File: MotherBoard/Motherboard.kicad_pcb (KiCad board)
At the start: 2 copper layers, 63.5 x 46.4 mm, 31 parts, among them J1 22-28-4157, J2 X6521WV-2x15H-C60D30, Q1 NCE2302, SW1 FSM4JSMATR, SW2 FSM4JSMATR, U1 ESP32 S3, U2 Unidirectional 5.5V 6V SOT-14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, U4 LIS2MDLTR, U5 LIS3DHTR, U6 MAX7219M/TR, U7 C193852

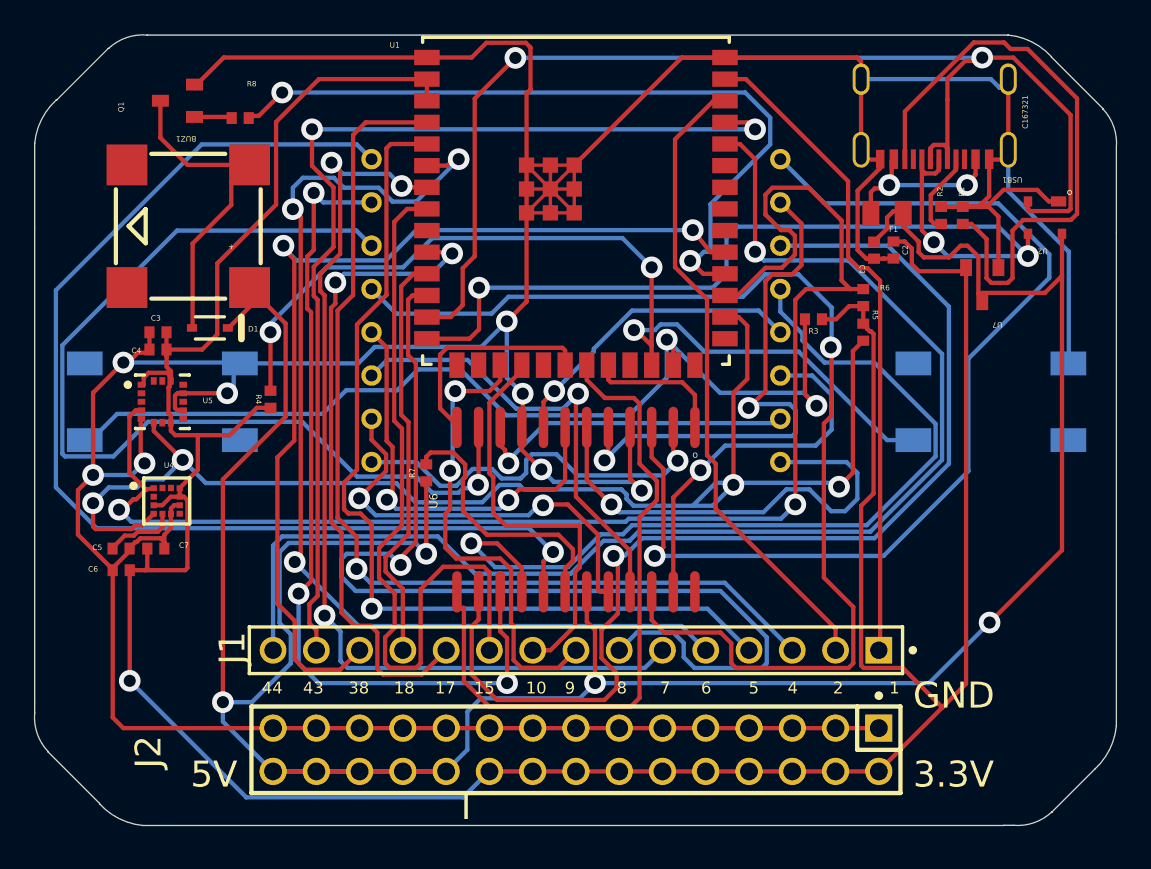
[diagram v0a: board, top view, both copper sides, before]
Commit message: motherboard imported and corrected
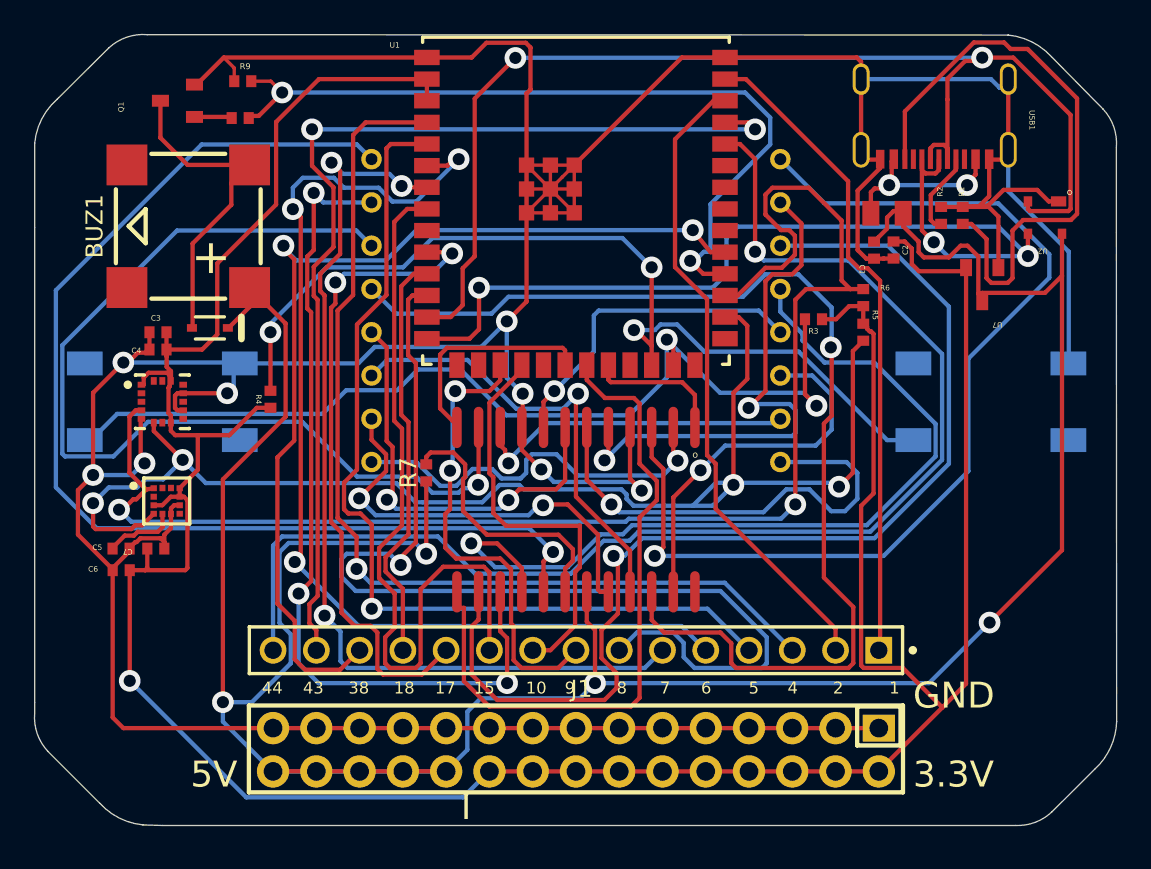
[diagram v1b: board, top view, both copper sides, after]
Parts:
- added R9: 10K, FableFootPrintLibrary:0402R, F.Cu at (129.0, 84.5)
- BUZ1: footprint BUZ-SMD_4P-L8.5-W8.5-P8.50-BR:BUZ-SMD_4P-L8.5-W8.5-P8.50-BR -> FableFootPrintLibrary:BUZ-SMD_4P-L8.5-W8.5-P8.50-BR
- C7: value 22pF -> 10uF
- D1: footprint Vault:DIOD-SOD323-2-A_V -> FableFootPrintLibrary:DIOD-SOD323-2-A_V
- F1: footprint Hub 2.0:0805 -> FableFootPrintLibrary:0805
- J1: footprint Vault:FP-22-28-4157-MFG -> FableFootPrintLibrary:FP-22-28-4157-MFG
- J2: footprint HDR-TH_30P-P2.54-V-M-R2-C15-S2.54-BL:HDR-TH_30P-P2.54-V-M-R2-C15-S2.54-BL -> FableFootPrintLibrary:HDR-TH_30P-P2.54-V-F-R2-C15-S2.54
- L1: footprint LED-SEG-TH_SZ421288N-64:LED-SEG-TH_SZ421288N-64 -> FableFootPrintLibrary:LED-SEG-TH_SZ421288N-64
- R7, R8: footprint Hub 2.0:0402R -> FableFootPrintLibrary:0402R
- SW1, SW2: footprint Vault:TECO-FSM4JSMATR_V -> FableFootPrintLibrary:TECO-FSM4JSMATR_V
- U4: footprint Vault:FP-LGA-12-DM00170568-MFG -> FableFootPrintLibrary:FP-LGA-12-DM00170568-MFG
- U5: footprint Vault:FP-LGA-16-7983231-MFG -> FableFootPrintLibrary:FP-LGA-16-7983231-MFG
- U6: footprint SOP-24_L15.4-W7.5-P1.27-LS10.4-BL:SOP-24_L15.4-W7.5-P1.27-LS10.4-BL -> FableFootPrintLibrary:SOP-24_L15.4-W7.5-P1.27-LS10.4-BL
- turned C7 to 180 degrees
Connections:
- net NetBUZ1_2 renamed Net-(D1-A)
- net NetC5_1 renamed Net-(U4-C1)
- net NetJ1_1 renamed /IO01
- net NetJ1_10 renamed /IO15
- net NetJ1_11 renamed /IO17
- net NetJ1_12 renamed /IO18
- net NetJ1_13 renamed /IO38
- net NetJ1_14 renamed /IO43
- net NetJ1_15 renamed /IO44
- net NetJ1_2 renamed /IO02
- net NetJ1_3 renamed /IO4
- net NetJ1_4 renamed /IO5
- net NetJ1_5 renamed /IO6
- net NetJ1_6 renamed /IO7
- net NetJ1_7 renamed /IO8
- net NetJ1_8 renamed /IO9
- net NetJ1_9 renamed /IO10
- net NetL1_1 renamed /DIG4
- net NetL1_10 renamed /SEGC
- net NetL1_11 renamed /SEGE
- net NetL1_12 renamed /DIG3
- net NetL1_13 renamed /SEGDP
- net NetL1_14 renamed /DIG1
- net NetL1_15 renamed /SEGF
- net NetL1_16 renamed /SEGG
- net NetL1_2 renamed /DIG6
- net NetL1_3 renamed /SEGA
- net NetL1_4 renamed /SEGB
- net NetL1_5 renamed /DIG7
- net NetL1_6 renamed /SEGD
- net NetL1_7 renamed /DIG5
- net NetL1_8 renamed /DIG2
- net NetL1_9 renamed /DIG0
- net NetQ1_1 renamed Net-(Q1-G)
- net NetR1_2 renamed Net-(USB1-CC2)
- net NetR2_2 renamed Net-(USB1-CC1)
- net NetR3_1 renamed /B1
- net NetR4_1 renamed /B2
- net NetR5_2 renamed /SDA
- net NetR6_2 renamed /SCL
- net NetR7_2 renamed Net-(U6-ISET)
- net NetR8_2 renamed /BUZZER_SIG
- net NetU1_19 renamed /IO11
- net NetU1_20 renamed /IO12
- net NetU1_21 renamed /IO13
- net NetU1_22 renamed /IO14
- net NetU1_9 renamed /IO16
- net fuse renamed /fuse
- BUZ1 pad 3: (no net) -> unconnected-(BUZ1-Pad3)
- BUZ1 pad 4: (no net) -> unconnected-(BUZ1-Pad4)
- C7 pad 1: +3.3 -> GND
- C7 pad 2: GND -> +3.3
- SW1 pad 2: (no net) -> unconnected-(SW1-Pad2)
- SW1 pad 3: (no net) -> unconnected-(SW1-Pad3)
- SW2 pad 2: (no net) -> unconnected-(SW2-Pad2)
- SW2 pad 3: (no net) -> unconnected-(SW2-Pad3)
- U1 pad 15: (no net) -> unconnected-(U1C-JTAG_SRC_(IO3)-Pad15)
- U1 pad 16: (no net) -> unconnected-(U1C-Boot_(IO46)-Pad16)
- U1 pad 23: (no net) -> unconnected-(U1A-IO21-Pad23)
- U1 pad 26: (no net) -> unconnected-(U1C-VDD_SPI_(IO45)-Pad26)
- U1 pad 27: (no net) -> unconnected-(U1C-Boot_(IO0)-Pad27)
- U1 pad 32: (no net) -> unconnected-(U1D-TCK_(IO39)-Pad32)
- U1 pad 33: (no net) -> unconnected-(U1D-TDO_(IO40)-Pad33)
- U1 pad 34: (no net) -> unconnected-(U1D-TDI_(IO41)-Pad34)
- U1 pad 35: (no net) -> unconnected-(U1D-TMS_(IO42)-Pad35)
- U4 pad 11: (no net) -> unconnected-(U4-NC-Pad11)
- U4 pad 12: (no net) -> unconnected-(U4-NC-Pad12)
- U4 pad 2: (no net) -> unconnected-(U4-NC-Pad2)
- U4 pad 7: (no net) -> unconnected-(U4-INT/DRDY/SDO-Pad7)
- U5 pad 11: (no net) -> unconnected-(U5-INT1-Pad11)
- U5 pad 13: (no net) -> unconnected-(U5-ADC3-Pad13)
- U5 pad 15: (no net) -> unconnected-(U5-ADC2-Pad15)
- U5 pad 16: (no net) -> unconnected-(U5-ADC1-Pad16)
- U5 pad 2: (no net) -> unconnected-(U5-NC-Pad2)
- U5 pad 3: (no net) -> unconnected-(U5-NC-Pad3)
- U5 pad 7: (no net) -> unconnected-(U5-SDO/SA0-Pad7)
- U5 pad 9: (no net) -> unconnected-(U5-INT2-Pad9)
- U6 pad 24: (no net) -> unconnected-(U6-DOUT-Pad24)
- USB1 pad A8: (no net) -> unconnected-(USB1-SBU1-PadA8)
- USB1 pad B8: (no net) -> unconnected-(USB1-SBU2-PadB8)
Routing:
- net /BUZZER_SIG: track 44.5 -> 46.6 mm
- net GND: track 275.9 -> 277.5 mm
- net /DIG7: track 18.2 -> 19.4 mm
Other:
- outline, holes or cut-outs redrawn
- copper layers 2 -> 4
